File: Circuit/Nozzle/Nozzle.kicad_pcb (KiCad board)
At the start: 2 copper layers, 70 x 70 mm, 6 parts, among them J1 Coil Power

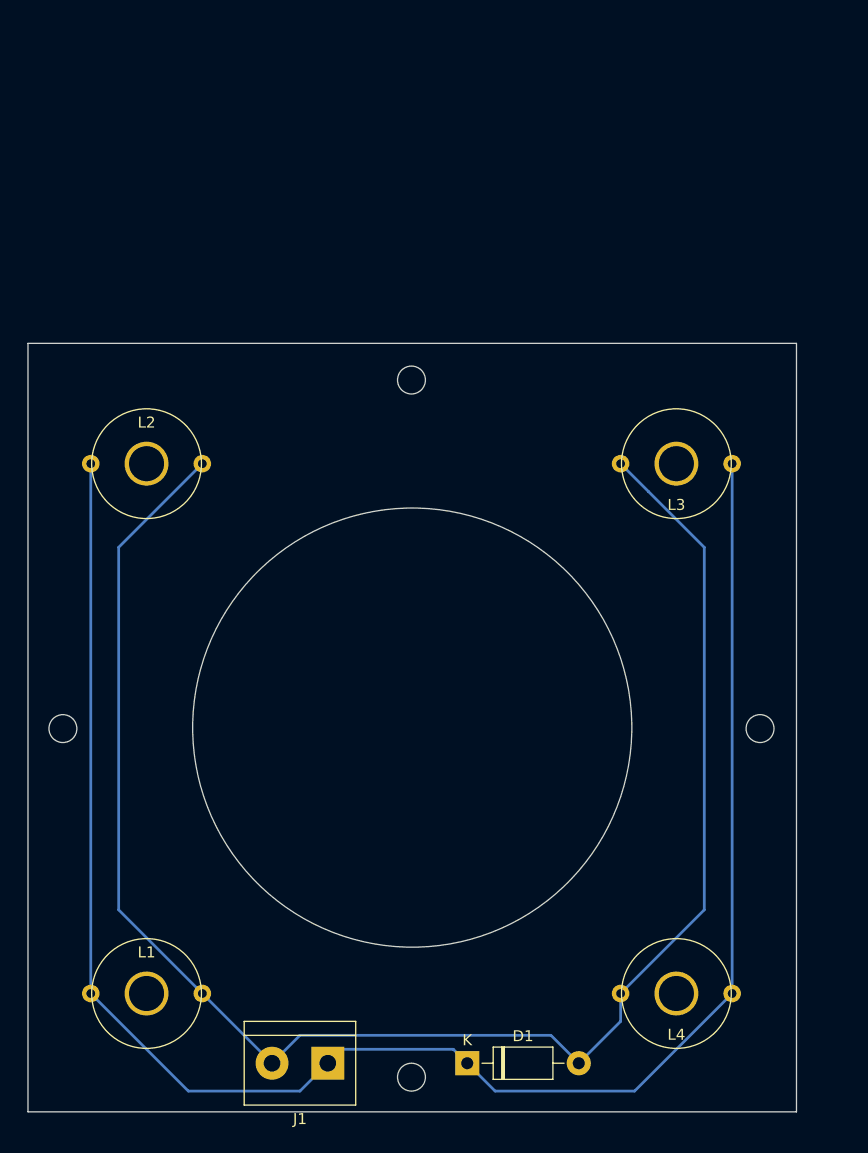
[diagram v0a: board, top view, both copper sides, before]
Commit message: [Circuit] Adjust the nozzle PCB
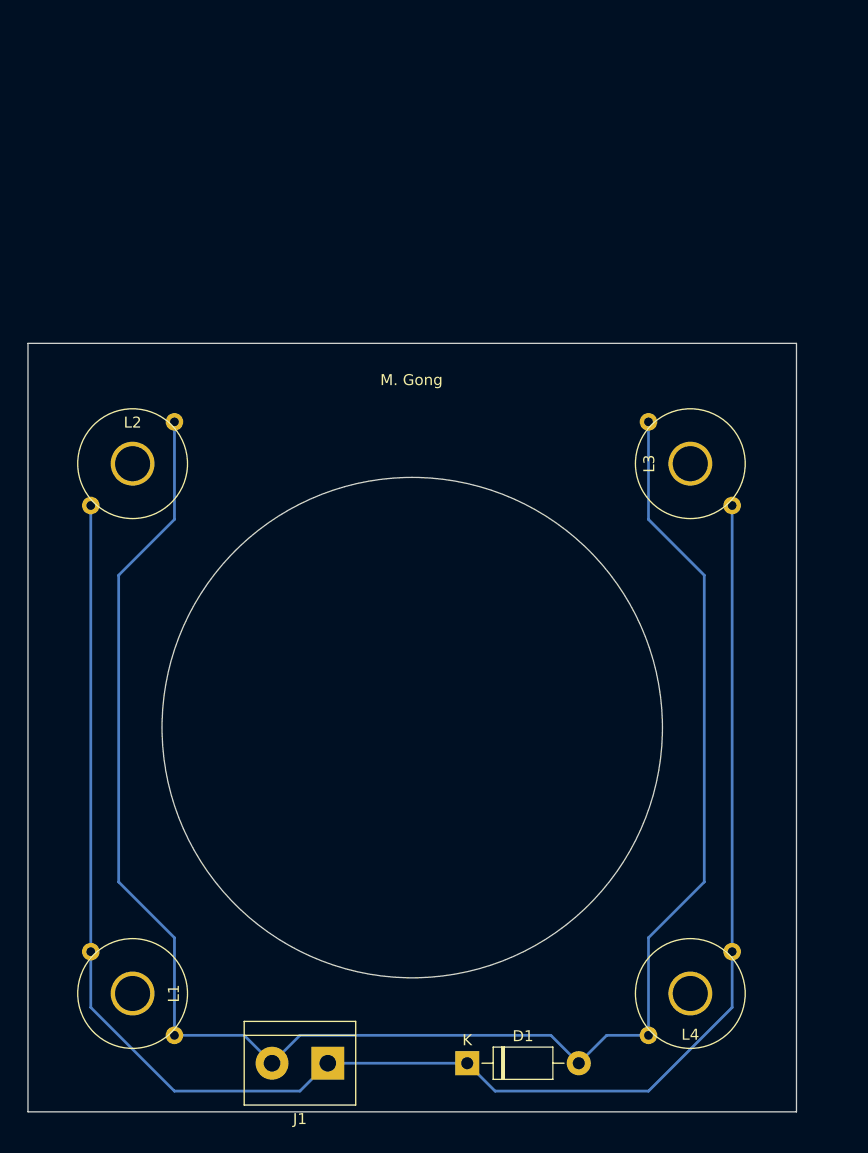
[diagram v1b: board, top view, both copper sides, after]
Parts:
- moved L1 1.27 mm to (49.5, 109.2), turned to 270 degrees
- moved L2 1.27 mm to (49.5, 61.0)
- moved L3 1.27 mm to (100.3, 61.0), turned to 90 degrees
- moved L4 1.27 mm to (100.3, 109.2)
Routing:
- net /CoilPower-: track 156.1 -> 167.6 mm
- net /CoilPower+: track 165.5 -> 158.3 mm
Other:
- outline, holes or cut-outs redrawn
- board text added: "M. Gong"

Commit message: [Circuit] Use thick tracks in nozzle PCB
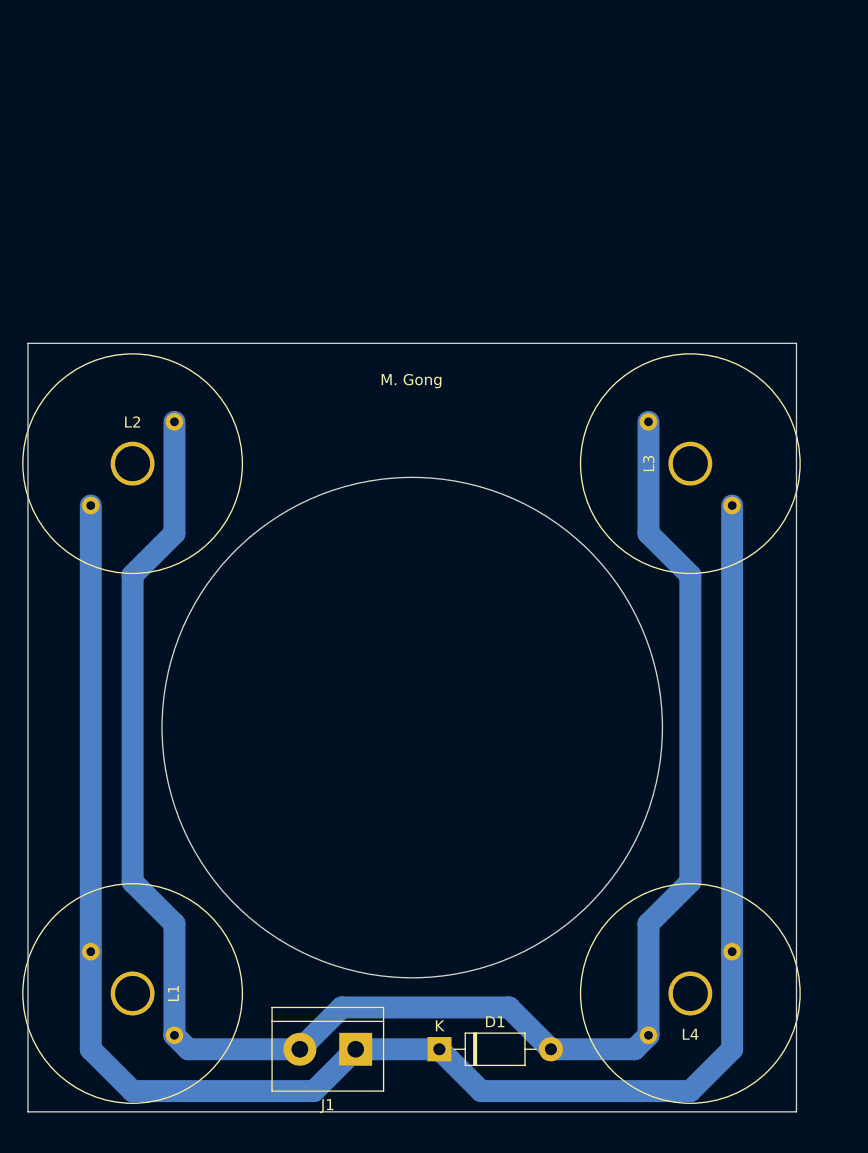
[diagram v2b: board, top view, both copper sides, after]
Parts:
- moved D1 2.84 mm to (77.5, 114.3)
- moved J1 2.84 mm to (69.8, 114.3)
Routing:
- net /CoilPower+: track 158.3 -> 163.8 mm
- net /CoilPower-: track 167.6 -> 165.5 mm

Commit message: [Circuit] Add a capacitor bank for EMs in nozzle
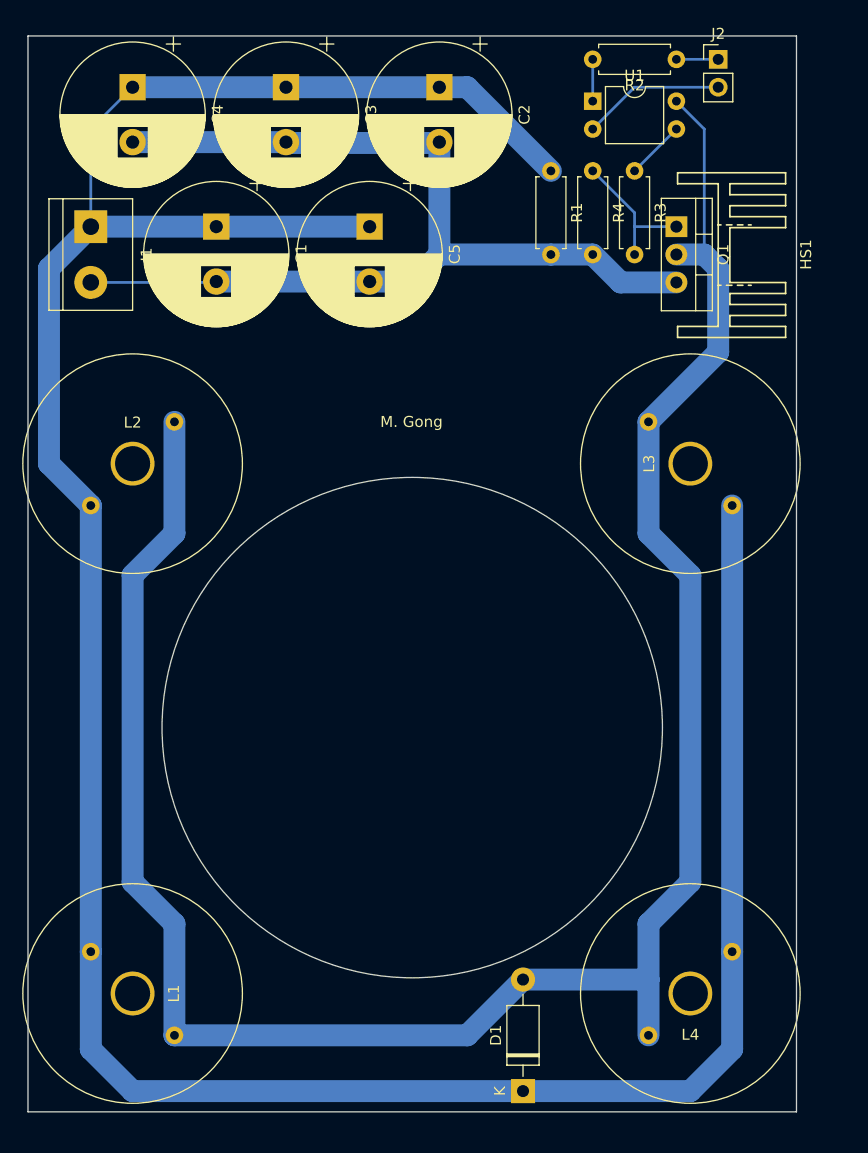
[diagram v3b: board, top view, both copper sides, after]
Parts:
- added C1: 2200uF, Capacitor_THT:CP_Radial_D13.0mm_P5.00mm, F.Cu at (57.1, 39.4)
- added C2: 2200uF, Capacitor_THT:CP_Radial_D13.0mm_P5.00mm, F.Cu at (77.5, 26.7)
- added C3: 2200uF, Capacitor_THT:CP_Radial_D13.0mm_P5.00mm, F.Cu at (63.5, 26.7)
- added C4: 2200uF, Capacitor_THT:CP_Radial_D13.0mm_P5.00mm, F.Cu at (49.5, 26.7)
- added C5: 2200uF, Capacitor_THT:CP_Radial_D13.0mm_P5.00mm, F.Cu at (71.1, 39.4)
- added HS1: Heatsink, Nozzle:Heatsink_TO220_15x10mm, F.Cu at (102.9, 41.9)
- added J2: Conn_01x02_Male, Connector_PinHeader_2.54mm:PinHeader_1x02_P2.54mm_Vertical, F.Cu at (102.9, 24.1)
- added Q1: RFP30N06LE, Package_TO_SOT_THT:TO-220-3_Vertical, F.Cu at (99.1, 39.4)
- added R1: 5.1K, Resistor_THT:R_Axial_DIN0207_L6.3mm_D2.5mm_P7.62mm_Horizontal, F.Cu at (87.6, 34.3)
- added R2: 1K, Resistor_THT:R_Axial_DIN0207_L6.3mm_D2.5mm_P7.62mm_Horizontal, F.Cu at (99.1, 24.1)
- added R3: 10K, Resistor_THT:R_Axial_DIN0207_L6.3mm_D2.5mm_P7.62mm_Horizontal, F.Cu at (95.2, 34.3)
- added R4: 10K, Resistor_THT:R_Axial_DIN0207_L6.3mm_D2.5mm_P7.62mm_Horizontal, F.Cu at (91.4, 34.3)
- added U1: PC817, Package_DIP:DIP-4_W7.62mm, F.Cu at (91.4, 27.9)
- moved J1 78.7 mm to (45.7, 39.4), turned to 270 degrees
- moved D1 8.52 mm to (85.1, 118.1), turned to 90 degrees
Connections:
- D1 pad 2: /CoilPower- -> Net-(D1-Pad2)
- L1 pad 2: /CoilPower- -> Net-(D1-Pad2)
- L2 pad 2: /CoilPower- -> Net-(D1-Pad2)
- L3 pad 2: /CoilPower- -> Net-(D1-Pad2)
- L4 pad 2: /CoilPower- -> Net-(D1-Pad2)
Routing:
- net Net-(D1-Pad2): track 0.00 -> 199.3 mm
- net /CoilPower+: track 163.8 -> 270.1 mm
- net /CoilPower-: track 165.5 -> 92.4 mm
- net /CoilSignal-: track 0.00 -> 13.0 mm
- net Net-(Q1-Pad1): track 0.00 -> 13.0 mm
- net Net-(R3-Pad1): track 0.00 -> 5.39 mm
- net Net-(R2-Pad2): track 0.00 -> 3.81 mm
- net /CoilSignal+: track 0.00 -> 3.81 mm
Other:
- board size 70 x 70 mm -> 70 x 98 mm

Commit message: [Circuit] Add protection components for EM board
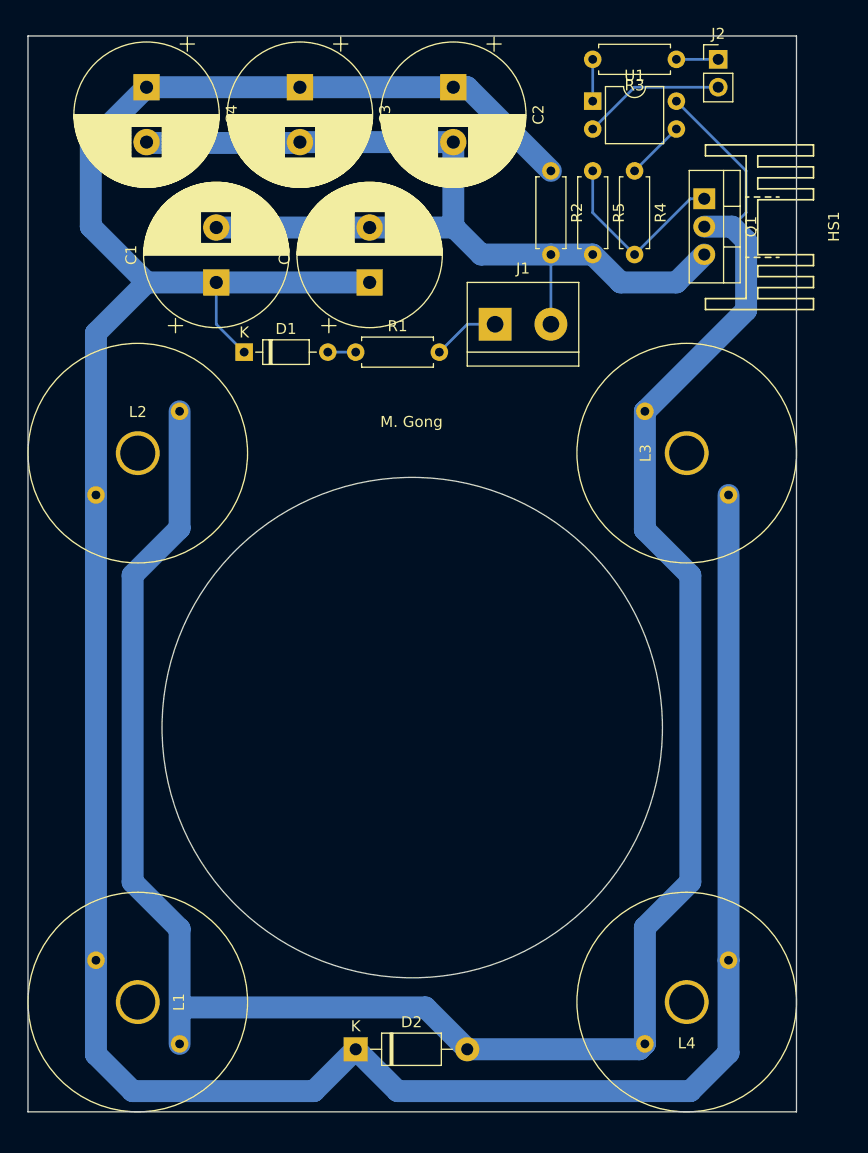
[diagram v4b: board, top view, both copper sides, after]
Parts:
- added D1: 1N4148, Diode_THT:D_DO-35_SOD27_P7.62mm_Horizontal, F.Cu at (59.7, 50.8)
- added R1: 220, Resistor_THT:R_Axial_DIN0207_L6.3mm_D2.5mm_P7.62mm_Horizontal, F.Cu at (69.8, 50.8)
- moved J1 37.9 mm to (82.5, 48.3), turned to 0 degrees
- moved D2 15.7 mm to (69.8, 114.3), turned to 0 degrees
- moved C1 5.08 mm to (57.1, 44.5), turned to 90 degrees
- moved C5 5.08 mm to (71.1, 44.5), turned to 90 degrees
- moved HS1 3.59 mm to (105.4, 39.4)
- moved Q1 3.59 mm to (101.6, 36.8)
- moved C2 1.27 mm to (78.7, 26.7)
- moved C3 1.27 mm to (64.8, 26.7)
- moved C4 1.27 mm to (50.8, 26.7)
- moved L2 1.07 mm to (50.0, 60.0)
- moved L3 1.02 mm to (100.0, 60.0)
- moved L1 0.91 mm to (50.0, 110.0)
- moved L4 0.85 mm to (100.0, 110.0)
- renumbered D1 to D2, R1 to R2, R2 to R3, R3 to R4, R4 to R5
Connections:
- C1 pad 1: /CoilPower+ -> Net-(C1-Pad1)
- C2 pad 1: /CoilPower+ -> Net-(C1-Pad1)
- C3 pad 1: /CoilPower+ -> Net-(C1-Pad1)
- C4 pad 1: /CoilPower+ -> Net-(C1-Pad1)
- C5 pad 1: /CoilPower+ -> Net-(C1-Pad1)
- D2 pad 1: /CoilPower+ -> Net-(C1-Pad1)
- L1 pad 1: /CoilPower+ -> Net-(C1-Pad1)
- L2 pad 1: /CoilPower+ -> Net-(C1-Pad1)
- L3 pad 1: /CoilPower+ -> Net-(C1-Pad1)
- L4 pad 1: /CoilPower+ -> Net-(C1-Pad1)
- R2 pad 1: /CoilPower+ -> Net-(C1-Pad1)
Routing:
- net Net-(C1-Pad1): track 0.00 -> 276.5 mm
- net /CoilPower+: track 270.1 -> 6.13 mm
- net Net-(D2-Pad2): track 199.3 -> 204.2 mm
- net Net-(Q1-Pad1): track 13.0 -> 17.7 mm
- net Net-(D1-Pad2): track 0.00 -> 2.54 mm
- net /CoilPower-: track 92.4 -> 89.9 mm

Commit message: [Circuit] Adjust the resistors in mosfet SSRs
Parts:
- J2: value Conn_01x02_Male -> CoilSignal
- moved R3 11.4 mm to (87.6, 24.1), turned to 0 degrees
- moved R4 7.62 mm to (95.2, 41.9), turned to 90 degrees
- moved J2 3.81 mm to (99.1, 24.1)
- moved U1 3.81 mm to (87.6, 27.9)
- moved HS1 2.54 mm to (102.9, 39.4)
- moved Q1 2.54 mm to (99.1, 36.8)
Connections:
- R3 pad 1: /CoilSignal+ -> Net-(R3-Pad1)
- R3 pad 2: Net-(R3-Pad2) -> /CoilSignal+
- R4 pad 1: Net-(R4-Pad1) -> Net-(C1-Pad1)
- R4 pad 2: Net-(Q1-Pad1) -> Net-(R4-Pad2)
- U1 pad 1: Net-(R3-Pad2) -> Net-(R3-Pad1)
- U1 pad 3: Net-(R4-Pad1) -> Net-(Q1-Pad1)
- U1 pad 4: Net-(D2-Pad2) -> Net-(R4-Pad2)
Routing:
- net Net-(D2-Pad2): track 204.2 -> 186.8 mm
- net Net-(C1-Pad1): track 276.5 -> 287.2 mm
- net Net-(R4-Pad2): track 0.00 -> 7.40 mm
- net Net-(R4-Pad1): track 5.39 -> 0.00 mm
- net Net-(R3-Pad2): track 3.81 -> 0.00 mm
- net Net-(R3-Pad1): track 0.00 -> 3.81 mm
- net Net-(Q1-Pad1): track 17.7 -> 14.1 mm
- net /CoilPower-: track 89.9 -> 87.3 mm

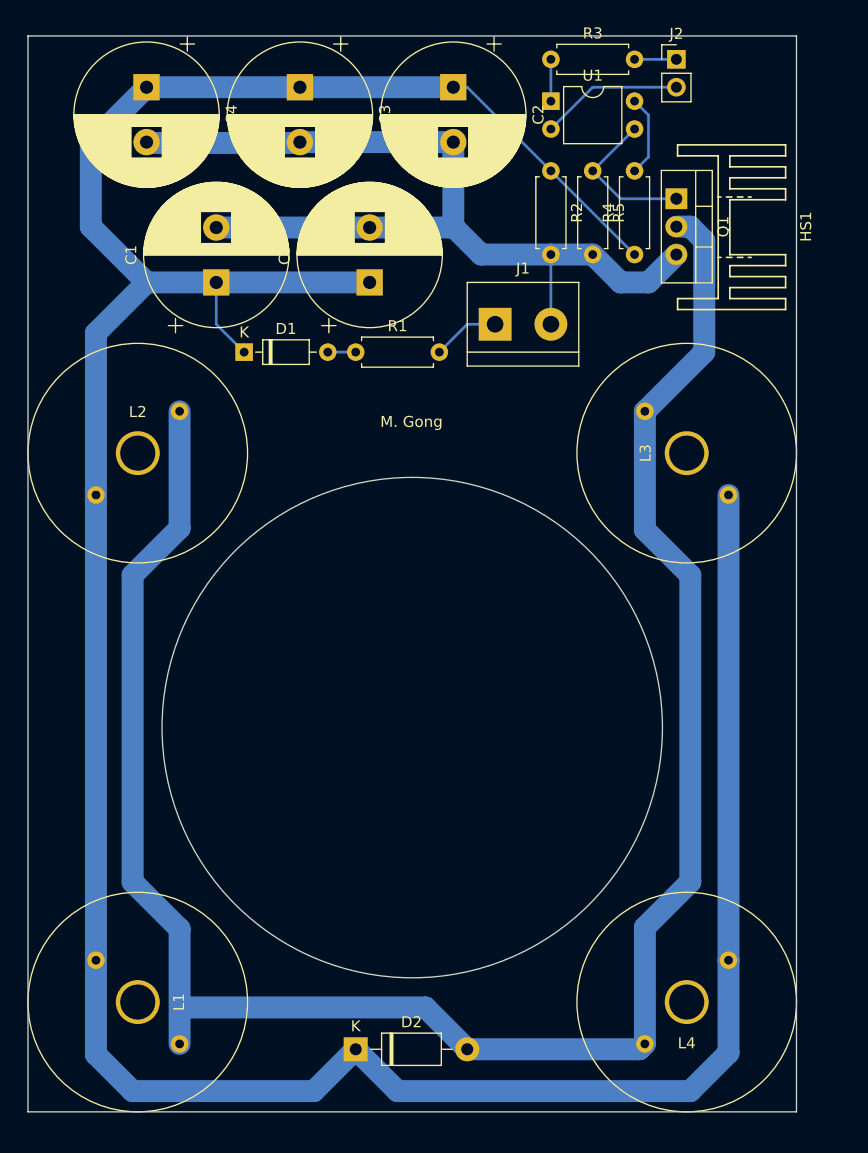
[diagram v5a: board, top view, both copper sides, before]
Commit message: [Circuit] Use 2 big capacitors to replace 5 small ones
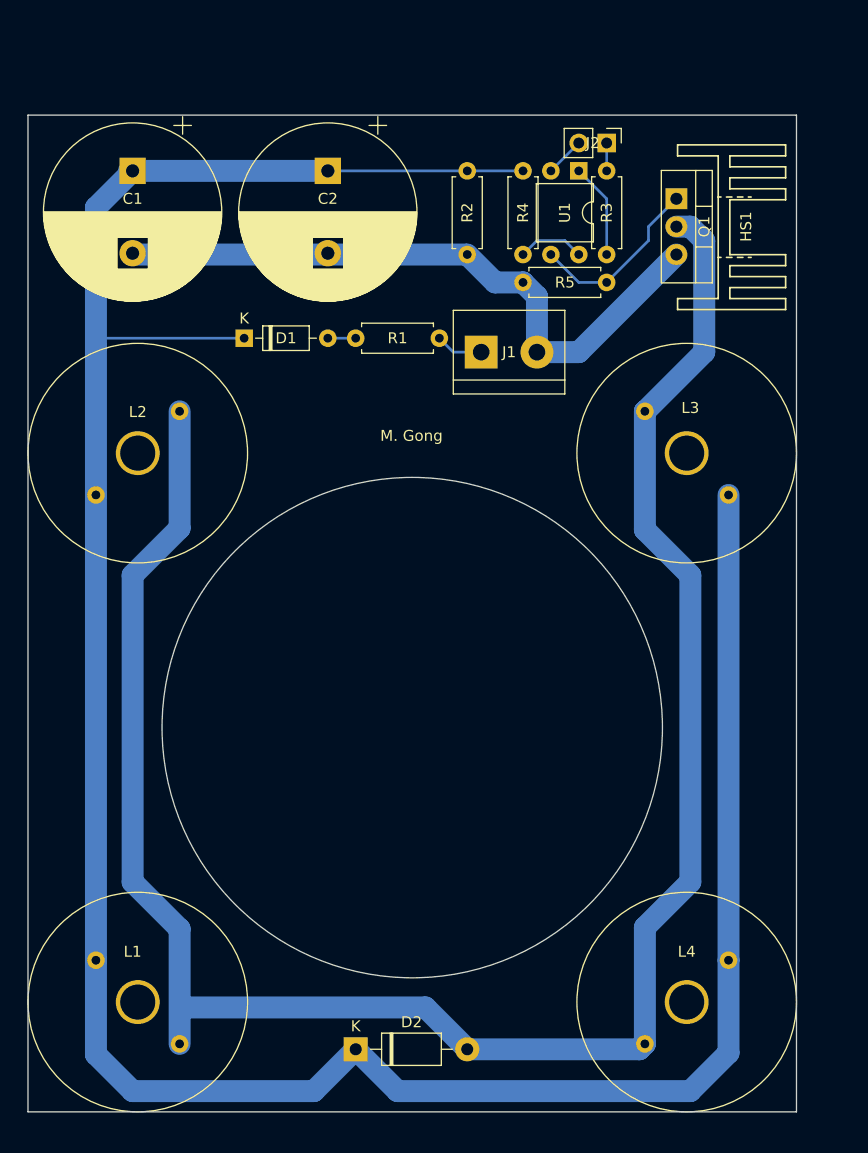
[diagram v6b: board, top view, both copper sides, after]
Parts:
- removed C3, C4, C5: 2200uF, Capacitor_THT:CP_Radial_D13.0mm_P5.00mm
- C1, C2: value 2200uF -> 4700uF; footprint Capacitor_THT:CP_Radial_D13.0mm_P5.00mm -> Capacitor_THT:CP_Radial_D16.0mm_P7.50mm
- moved R3 18.5 mm to (92.7, 41.9), turned to 90 degrees
- moved C2 13.7 mm to (67.3, 34.3)
- moved C1 12.7 mm to (49.5, 34.3), turned to 270 degrees
- moved R4 12.7 mm to (85.1, 34.3), turned to 270 degrees
- moved R5 10.2 mm to (92.7, 44.5), turned to 180 degrees
- moved J2 9.92 mm to (92.7, 31.8), turned to 270 degrees
- moved R2 7.62 mm to (80.0, 34.3)
- moved U1 6.84 mm to (90.2, 34.3), turned to 270 degrees
- moved J1 2.84 mm to (81.3, 50.8)
- moved D1 1.27 mm to (59.7, 49.5)
- moved R1 1.27 mm to (69.8, 49.5)
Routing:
- net Net-(C1-Pad1): track 287.2 -> 246.0 mm
- net /CoilPower-: track 87.3 -> 59.8 mm
- net /CoilSignal-: track 13.0 -> 3.59 mm
- net Net-(R3-Pad1): track 3.81 -> 8.67 mm
- net Net-(Q1-Pad1): track 14.1 -> 16.4 mm
- net /CoilPower+: track 6.13 -> 4.34 mm
- net /CoilSignal+: track 3.81 -> 2.54 mm
- net Net-(R4-Pad2): track 7.40 -> 6.13 mm
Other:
- board size 70 x 98 mm -> 70 x 90.8 mm
